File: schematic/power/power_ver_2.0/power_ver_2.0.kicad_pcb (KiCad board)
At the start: 2 copper layers, 5 parts, among them Q1 RFP12N10L, Q2 RFP12N10L, Q3 RFP12N10L, Q4 RFP12N10L, U1 HIP4082IP

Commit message: ver2 pcb layout
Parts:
- added C1: ECE-A1HN101U, Capacitor_THT:CP_Radial_D10.0mm_P5.00mm, F.Cu at (109.0, 95.1)
- added C10: C324C106K3R5TA, Capacitor_THT:C_Radial_D4.0mm_H5.0mm_P1.50mm, F.Cu at (105.8, 72.9)
- added C11: SR205C104MAATR1, Capacitor_THT:C_Radial_D4.0mm_H5.0mm_P1.50mm, F.Cu at (105.8, 80.5)
- added C2: C324C106K3R5TA, Capacitor_THT:C_Radial_D4.0mm_H5.0mm_P1.50mm, F.Cu at (112.1, 105.3)
- added C3: SR205C104MAATR1, Capacitor_THT:C_Radial_D4.0mm_H5.0mm_P1.50mm, F.Cu at (104.5, 105.3)
- added C4: ECE-A1HN100U, Capacitor_THT:CP_Radial_D6.3mm_P2.50mm, F.Cu at (140.2, 115.8)
- added C5: ECE-A1HN100U, Capacitor_THT:CP_Radial_D6.3mm_P2.50mm, F.Cu at (108.7, 115.8)
- added C6: C324C106K3R5TA, Capacitor_THT:C_Radial_D4.0mm_H5.0mm_P1.50mm, F.Cu at (182.6, 132.1)
- added C7: C324C106K3R5TA, Capacitor_THT:C_Radial_D4.0mm_H5.0mm_P1.50mm, F.Cu at (162.3, 118.0)
- added C8: EEU-FC1H102L, Capacitor_THT:CP_Radial_D12.5mm_P5.00mm, F.Cu at (93.7, 79.9)
- added C9: C324C106K3R5TA, Capacitor_THT:C_Radial_D4.0mm_H5.0mm_P1.50mm, F.Cu at (182.6, 102.1)
- added D1: 1N4148, Diode_THT:D_DO-35_SOD27_P7.62mm_Horizontal, F.Cu at (124.2, 111.0)
- added D2: 1N4148, Diode_THT:D_DO-35_SOD27_P7.62mm_Horizontal, F.Cu at (117.2, 111.0)
- added D3: 1N4148, Diode_THT:D_DO-35_SOD27_P7.62mm_Horizontal, F.Cu at (117.2, 86.9)
- added D4: 1N4148, Diode_THT:D_DO-35_SOD27_P7.62mm_Horizontal, F.Cu at (136.9, 86.9)
- added D5: 1N4148, Diode_THT:D_DO-35_SOD27_P7.62mm_Horizontal, F.Cu at (177.5, 87.5)
- added D6: 1N4148, Diode_THT:D_DO-35_SOD27_P7.62mm_Horizontal, F.Cu at (156.6, 86.9)
- added J1: PWM INPUT, TerminalBlock:TerminalBlock_Altech_AK300-2_P5.00mm, F.Cu at (132.5, 138.2)
- added J2: Audio OUTPUT, TerminalBlock:TerminalBlock_Altech_AK300-2_P5.00mm, F.Cu at (182.6, 121.2)
- added J3: OUTPUT Power, TerminalBlock:TerminalBlock_Altech_AK300-2_P5.00mm, F.Cu at (93.5, 95.1)
- added J4: PWM_power, TerminalBlock:TerminalBlock_Altech_AK300-2_P5.00mm, F.Cu at (117.3, 138.2)
- added L1: 2216-V-RC, Inductor_THT:L_Toroid_Vertical_L24.6mm_W15.5mm_P11.44mm_Pulse_KM-4, F.Cu at (162.3, 136.4)
- added L2: 2216-V-RC, Inductor_THT:L_Toroid_Vertical_L24.6mm_W15.5mm_P11.44mm_Pulse_KM-4, F.Cu at (162.3, 111.6)
- added R1: 1K, Resistor_THT:R_Axial_DIN0207_L6.3mm_D2.5mm_P10.16mm_Horizontal, F.Cu at (131.2, 109.7)
- added R2: R, Resistor_THT:R_Axial_DIN0207_L6.3mm_D2.5mm_P10.16mm_Horizontal, F.Cu at (111.5, 79.2)
- added R3: R, Resistor_THT:R_Axial_DIN0207_L6.3mm_D2.5mm_P10.16mm_Horizontal, F.Cu at (131.2, 79.2)
- added R4: R, Resistor_THT:R_Axial_DIN0207_L6.3mm_D2.5mm_P10.16mm_Horizontal, F.Cu at (122.9, 79.2)
- added R5: R, Resistor_THT:R_Axial_DIN0207_L6.3mm_D2.5mm_P10.16mm_Horizontal, F.Cu at (142.6, 79.2)
- added R6: R, Resistor_THT:R_Axial_DIN0207_L6.3mm_D2.5mm_P10.16mm_Horizontal, F.Cu at (183.3, 79.2)
- added R7: R, Resistor_THT:R_Axial_DIN0207_L6.3mm_D2.5mm_P10.16mm_Horizontal, F.Cu at (162.3, 89.4)
- added R8: R, Resistor_THT:R_Axial_DIN0207_L6.3mm_D2.5mm_P10.16mm_Horizontal, F.Cu at (171.8, 89.4)
- added R9: R, Resistor_THT:R_Axial_DIN0207_L6.3mm_D2.5mm_P10.16mm_Horizontal, F.Cu at (150.9, 89.4)
- moved Q1 51.8 mm to (114.7, 72.9)
- moved Q2 45.0 mm to (134.4, 72.9)
- moved Q4 35.6 mm to (174.4, 72.9)
- moved Q3 32.9 mm to (154.1, 72.9)
- moved U1 24.9 mm to (120.4, 105.9), turned to 90 degrees
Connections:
- Q1 pad 2: Net-(Q1-Pad2) -> +15V
- Q1 pad 3: Net-(Q1-Pad3) -> Net-(C5-Pad2)
- Q2 pad 2: Net-(Q2-Pad2) -> Net-(C5-Pad2)
- Q2 pad 3: Net-(Q2-Pad3) -> GND
- Q3 pad 2: Net-(Q3-Pad2) -> +15V
- Q3 pad 3: Net-(Q3-Pad3) -> Net-(C4-Pad1)
- Q4 pad 2: Net-(Q4-Pad2) -> Net-(C4-Pad1)
- Q4 pad 3: Net-(Q4-Pad3) -> GND
- U1 pad 11: Net-(U1-Pad11) -> Net-(C4-Pad1)
- U1 pad 12: Net-(U1-Pad12) -> +15V
- U1 pad 15: Net-(U1-Pad15) -> Net-(C5-Pad2)
- U1 pad 2: Net-(U1-Pad2) -> +5V
- U1 pad 3: Net-(U1-Pad3) -> PWM+
- U1 pad 4: Net-(U1-Pad4) -> PWM-
- U1 pad 6: Net-(U1-Pad6) -> GND
- U1 pad 7: Net-(U1-Pad7) -> +5V
- U1 pad 8: Net-(U1-Pad8) -> GND
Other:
- board outline added: 109.2 x 83.8 mm

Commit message: auto roulting
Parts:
- moved L1 34.4 mm to (147.8, 105.2), turned to 90 degrees
- moved C6 27.9 mm to (156.0, 124.0), turned to 270 degrees
- moved J2 26.3 mm to (162.6, 138.2), turned to 0 degrees
- moved C9 23.2 mm to (174.8, 124.0), turned to 270 degrees
- moved L2 11.0 mm to (171.2, 105.2), turned to 90 degrees
- moved C7 6.59 mm to (165.1, 124.0)
- moved R1 6.13 mm to (130.6, 115.8)
- moved D1 4.83 mm to (124.2, 115.8)
- moved D2 4.83 mm to (117.2, 115.8)
- moved U1 3.30 mm to (120.4, 102.6)
- moved C11 1.27 mm to (105.8, 79.2)
- moved C8 0.68 mm to (93.5, 79.2), turned to 270 degrees
- moved C4 0.51 mm to (139.7, 115.8)
- moved C5 0.51 mm to (108.7, 116.3)
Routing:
- net GND: track 0.00 -> 280.6 mm
- net +15V: track 0.00 -> 176.6 mm
- net Net-(C4-Pad1): track 0.00 -> 118.8 mm
- net Net-(C5-Pad2): track 0.00 -> 110.7 mm
- net Net-(D5-Pad1): track 0.00 -> 56.1 mm
- net +5V: track 0.00 -> 50.1 mm
- net PWM+: track 0.00 -> 45.2 mm
- net Out+: track 0.00 -> 44.4 mm
- net Out-: track 0.00 -> 43.2 mm
- net Net-(C4-Pad2): track 0.00 -> 42.9 mm
- net PWM-: track 0.00 -> 38.2 mm
- net Net-(D5-Pad2): track 0.00 -> 25.0 mm
- net Net-(D3-Pad2): track 0.00 -> 24.9 mm
- net Net-(D4-Pad2): track 0.00 -> 24.8 mm
- net Net-(D6-Pad1): track 0.00 -> 24.6 mm
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
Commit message: finish pcb trace layout
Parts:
- added R10: 470, Resistor_THT:R_Axial_DIN0207_L6.3mm_D2.5mm_P10.16mm_Horizontal, F.Cu at (109.2, 131.1)
- added R11: 470, Resistor_THT:R_Axial_DIN0207_L6.3mm_D2.5mm_P10.16mm_Horizontal, F.Cu at (109.2, 136.1)
- C6, C7, C9: footprint Capacitor_THT:C_Radial_D4.0mm_H5.0mm_P1.50mm -> Capacitor_THT:C_Radial_D5.0mm_H11.0mm_P2.00mm
- J3: value OUTPUT Power -> Amp_Power
- J4: value PWM_power -> Driver_power
- Q1, Q2, Q3, Q4: value RFP12N10L -> IRF530A
- R2, R3, R8, R9: value R -> 100
- R4, R5, R6, R7: value R -> 10k
- moved R6 86.0 mm to (128.8, 145.8), turned to 0 degrees
- moved D5 72.2 mm to (129.5, 141.5), turned to 0 degrees
- moved Q4 72.2 mm to (147.6, 140.0), turned to 270 degrees
- moved R8 64.1 mm to (128.8, 136.9), turned to 0 degrees
- moved C8 56.4 mm to (149.6, 84.3)
- moved R7 54.3 mm to (128.8, 132.1), turned to 0 degrees
- moved Q3 53.2 mm to (147.6, 125.7), turned to 270 degrees
- moved D6 48.8 mm to (129.5, 127.5), turned to 0 degrees
- moved J1 45.1 mm to (87.9, 131.1), turned to 270 degrees
- moved C6 42.5 mm to (193.0, 103.1)
- moved R5 41.8 mm to (128.5, 118.6), turned to 0 degrees
- moved Q1 40.8 mm to (147.6, 97.0), turned to 270 degrees
- moved R9 40.4 mm to (128.8, 123.2), turned to 0 degrees
- moved Q2 39.8 mm to (147.6, 110.5), turned to 270 degrees
- moved J4 37.1 mm to (87.9, 115.6), turned to 270 degrees
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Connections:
- net Net-(C4-Pad1) renamed /A_HI
- net Net-(C5-Pad2) renamed /B_HI
- net Net-(D3-Pad1) renamed /BHO
- net Net-(D4-Pad1) renamed /BLO
- net Net-(D5-Pad1) renamed /ALO
- net Net-(D6-Pad1) renamed /AHO
- C1 pad 1: +15V -> +10V
- C2 pad 1: +15V -> +10V
- C3 pad 1: +15V -> +10V
- D1 pad 2: +15V -> +10V
- D2 pad 2: +15V -> +10V
- J2 pad 1: Out+ -> Out-
- J2 pad 2: Out- -> Out+
- J3 pad 1: GND -> +15V
- J3 pad 2: +15V -> GND
- J4 pad 2: +5V -> +10V
- U1 pad 12: +15V -> +10V
- U1 pad 2: +5V -> Net-(R11-Pad1)
- U1 pad 3: PWM+ -> Net-(R11-Pad1)
- U1 pad 4: PWM- -> Net-(R10-Pad1)
- U1 pad 7: +5V -> Net-(R10-Pad1)
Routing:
- net GND: track 280.6 -> 0.00 mm
- net +15V: track 176.6 -> 85.0 mm
- net +10V: track 0.00 -> 77.1 mm
- net +5V: track 50.1 -> 0.00 mm
- net /A_HI: track 118.8 -> 80.7 mm
- net /B_HI: track 110.7 -> 76.6 mm
- net PWM+: track 45.2 -> 11.2 mm
- net Net-(R11-Pad1): track 0.00 -> 31.2 mm
- net PWM-: track 38.2 -> 11.2 mm
- net /ALO: track 56.1 -> 31.6 mm
- net Net-(R10-Pad1): track 0.00 -> 21.1 mm
- net Net-(C4-Pad2): track 42.9 -> 25.2 mm
- net /AHO: track 24.6 -> 12.5 mm
- net Out-: track 43.2 -> 31.9 mm
- net Out+: track 44.4 -> 35.9 mm
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- added copper zone on B.Cu, net GND
- added copper zone on F.Cu, net GND
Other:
- board size 109.2 x 83.8 mm -> 127 x 76.2 mm
- board text added: "+10V"
- board text added: "+15V"
- board text added: "GND"
- board text added: "OUT+"
- board text added: "OUT-"
- board text added: "PWM+"
- board text added: "PWM-"

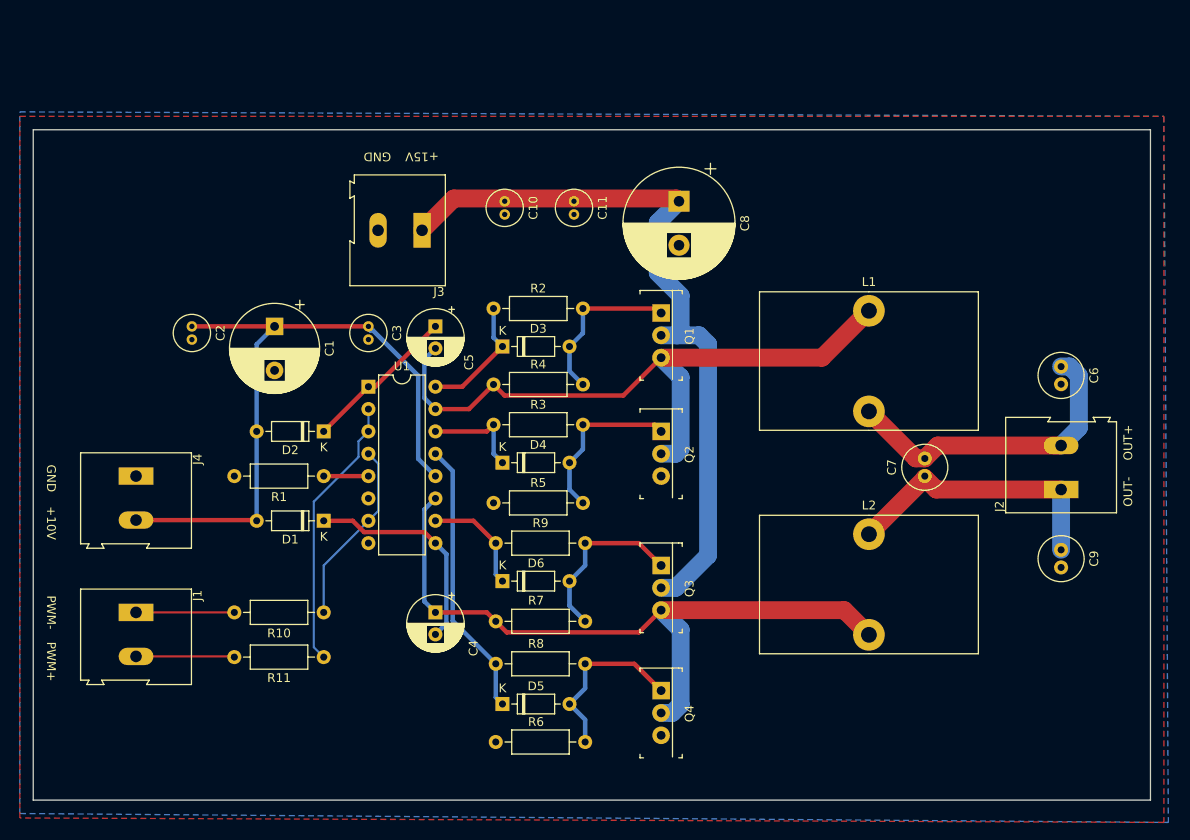
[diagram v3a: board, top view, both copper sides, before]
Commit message: add mounting hole, test point
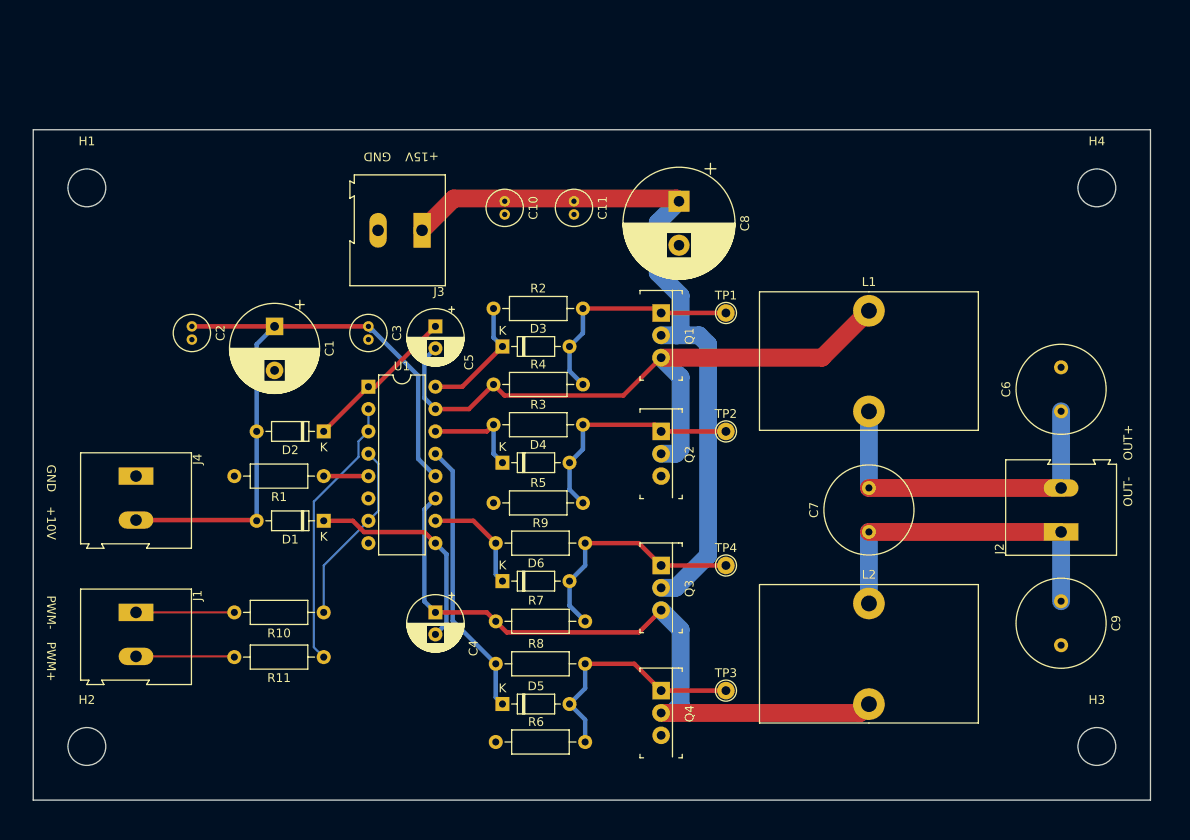
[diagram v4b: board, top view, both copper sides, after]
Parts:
- added H1: MountingHole, MountingHole:MountingHole_4.3mm_M4, F.Cu at (82.3, 82.8)
- added H2: MountingHole, MountingHole:MountingHole_4.3mm_M4, F.Cu at (82.3, 146.3)
- added H3: MountingHole, MountingHole:MountingHole_4.3mm_M4, F.Cu at (197.1, 146.3)
- added H4: MountingHole, MountingHole:MountingHole_4.3mm_M4, F.Cu at (197.1, 82.8)
- added TP1: TestPoint, TestPoint:TestPoint_THTPad_D2.0mm_Drill1.0mm, F.Cu at (154.9, 97.0)
- added TP2: TestPoint, TestPoint:TestPoint_THTPad_D2.0mm_Drill1.0mm, F.Cu at (154.9, 110.5)
- added TP3: TestPoint, TestPoint:TestPoint_THTPad_D2.0mm_Drill1.0mm, F.Cu at (154.9, 140.0)
- added TP4: TestPoint, TestPoint:TestPoint_THTPad_D2.0mm_Drill1.0mm, F.Cu at (154.9, 125.7)
- C6, C7, C9: footprint Capacitor_THT:C_Radial_D5.0mm_H11.0mm_P2.00mm -> Capacitor_THT:C_Radial_D10.0mm_H12.5mm_P5.00mm
- moved C7 8.98 mm to (171.2, 121.9)
- moved L2 7.87 mm to (171.2, 130.0)
- moved C9 5.84 mm to (193.0, 129.8)
- moved C6 5.08 mm to (193.0, 108.2), turned to 90 degrees
- moved J2 4.83 mm to (193.0, 121.9)
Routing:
- net Net-(D6-Pad2): track 20.1 -> 27.4 mm
- net Net-(D5-Pad2): track 20.3 -> 27.6 mm
- net Net-(D4-Pad2): track 19.4 -> 26.7 mm
- net Net-(D3-Pad2): track 19.0 -> 26.4 mm
- net Out-: track 31.9 -> 37.8 mm
- net Out+: track 35.9 -> 39.3 mm
- net /A_HI: track 80.7 -> 79.9 mm
- removed copper zone on B.Cu, net GND
- removed copper zone on F.Cu, net GND

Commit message: labels
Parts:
- C10, C11, C2, C3: footprint Capacitor_THT:C_Radial_D4.0mm_H5.0mm_P1.50mm -> Capacitor_THT:C_Disc_D3.8mm_W2.6mm_P2.50mm
- moved C10 32.3 mm to (162.1, 84.3)
- moved C11 32.0 mm to (169.7, 84.3)
- moved C6 1.27 mm to (191.8, 108.2)
- moved C9 1.27 mm to (191.8, 129.8)
- moved J2 1.27 mm to (191.8, 121.9)
- moved C2 0.36 mm to (94.5, 98.8)
- moved C3 0.25 mm to (114.3, 98.8)
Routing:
- net +15V: track 85.0 -> 105.0 mm
- net Out-: track 37.8 -> 36.6 mm
- net Out+: track 39.3 -> 38.0 mm
- added copper zone on B.Cu, net GND
- added copper zone on F.Cu, net GND
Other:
- board text added: "Amp_Power"
- board text added: "Audio_OUTPUT"
- board text added: "D_class Amplifier"
- board text added: "Driver_Power"
- board text added: "Load: 4 ohm"
- board text added: "PWM_INPUT"
- board text added: "Power: 80W Max"

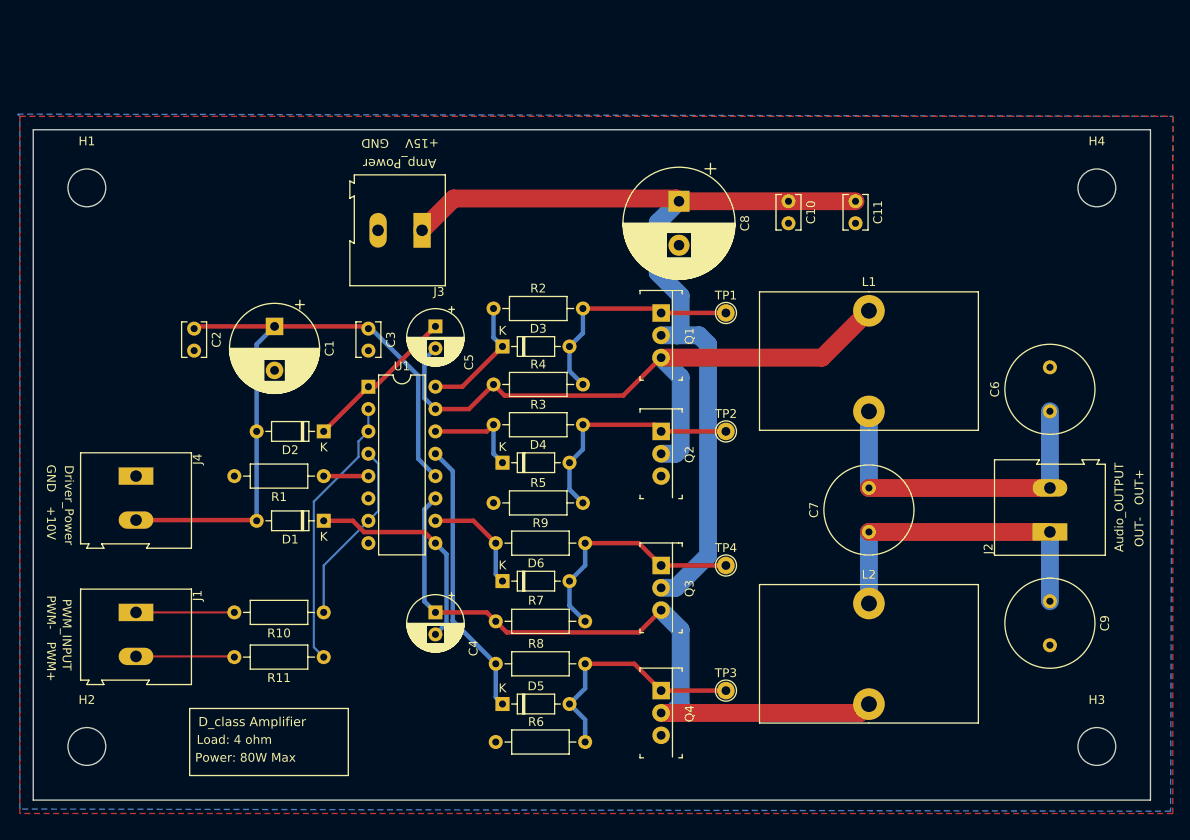
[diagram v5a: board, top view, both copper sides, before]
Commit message: add BOM
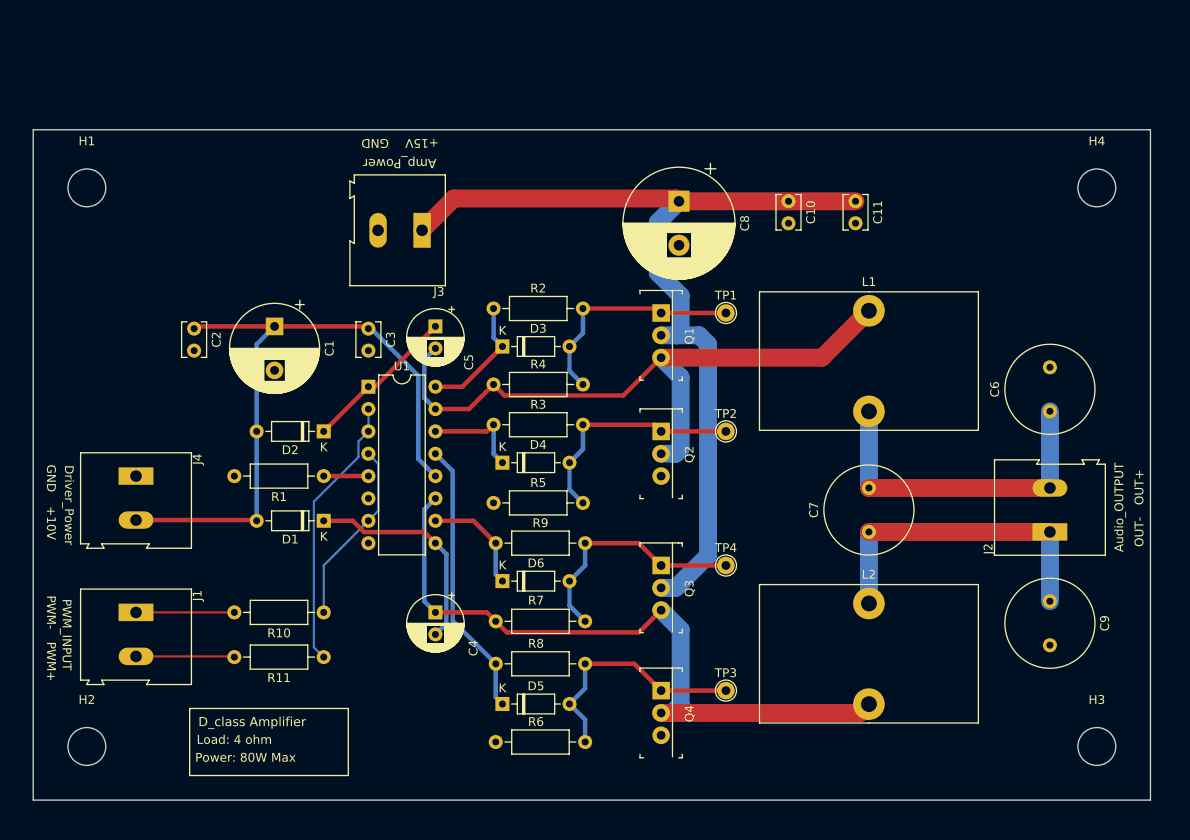
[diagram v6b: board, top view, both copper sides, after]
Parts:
- C11, C3: value SR205C104MAATR1 -> K104Z15Y5VE5TL2
- C4, C5: value ECE-A1HN100U -> ECA-1EM100B
- C6, C7, C9: value C324C106K3R5TA -> uF
- R1: value 1K -> MFP-25BRD52-1K
- R10, R11: value 470 -> CFR-25JB-52-470R
- R2, R3, R8, R9: value 100 -> CFR-25JR-52-100R
- R4, R5, R6, R7: value 10k -> CFR50SJT-52-10K
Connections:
- net /A_HI renamed Net-(C4-Pad1)
- net /B_HI renamed Net-(C5-Pad2)
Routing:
- removed copper zone on B.Cu, net GND
- removed copper zone on F.Cu, net GND
